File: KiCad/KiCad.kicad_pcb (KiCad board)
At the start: 2 copper layers, 43 parts, among them J1 Conn_01x03, J2 Conn_01x03, J3 Conn_01x03, J4 Screw_Terminal_01x02, J5 Screw_Terminal_01x02, Q1 2N3906, Q2 2N3906, Q3 2N3906, Q4 2N3904, Q5 2N3904, Q6 2N3904, U2 L298HN, U3 L7805, U4 ARDUINO_MKR_WAN_1310

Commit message: q
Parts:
- added C10: 0.1u, Capacitor_SMD:C_1206_3216Metric_Pad1.33x1.80mm_HandSolder, F.Cu at (131.7, 118.4)
- added C11: 0.1u, Capacitor_SMD:C_1206_3216Metric_Pad1.33x1.80mm_HandSolder, F.Cu at (131.7, 121.7)
- added C12: 0.1u, Capacitor_SMD:C_1206_3216Metric_Pad1.33x1.80mm_HandSolder, F.Cu at (131.7, 125.1)
- added C13: 0.1u, Capacitor_SMD:C_1206_3216Metric_Pad1.33x1.80mm_HandSolder, F.Cu at (131.7, 128.4)
- added C14: 0.1u, Capacitor_SMD:C_1206_3216Metric_Pad1.33x1.80mm_HandSolder, F.Cu at (131.7, 131.8)
- added C5: 0.1u, Capacitor_SMD:C_1206_3216Metric_Pad1.33x1.80mm_HandSolder, F.Cu at (125.7, 125.1)
- added C6: 0.1u, Capacitor_SMD:C_1206_3216Metric_Pad1.33x1.80mm_HandSolder, F.Cu at (125.7, 128.4)
- added C7: 0.1u, Capacitor_SMD:C_1206_3216Metric_Pad1.33x1.80mm_HandSolder, F.Cu at (125.7, 131.8)
- added C8: 0.1u, Capacitor_SMD:C_1206_3216Metric_Pad1.33x1.80mm_HandSolder, F.Cu at (131.7, 111.7)
- added C9: 0.1u, Capacitor_SMD:C_1206_3216Metric_Pad1.33x1.80mm_HandSolder, F.Cu at (131.7, 115.0)
- added D11: 1N5711UR, Diode_SMD:D_1206_3216Metric_Pad1.42x1.75mm_HandSolder, F.Cu at (148.8, 104.0)
- added D12: 1N5711UR, Diode_SMD:D_1206_3216Metric_Pad1.42x1.75mm_HandSolder, F.Cu at (148.8, 107.3)
- added D13: 1N4007, Diode_SMD:D_1206_3216Metric_Pad1.42x1.75mm_HandSolder, F.Cu at (148.8, 110.7)
- added D14: 1N4007, Diode_SMD:D_1206_3216Metric_Pad1.42x1.75mm_HandSolder, F.Cu at (148.8, 114.1)
- added D15: 1N4007, Diode_SMD:D_1206_3216Metric_Pad1.42x1.75mm_HandSolder, F.Cu at (148.8, 117.5)
- added D16: 1N4007, Diode_SMD:D_1206_3216Metric_Pad1.42x1.75mm_HandSolder, F.Cu at (148.8, 120.9)
- added D17: 1N4007, Diode_SMD:D_1206_3216Metric_Pad1.42x1.75mm_HandSolder, F.Cu at (148.8, 124.3)
- added D18: 1N4007, Diode_SMD:D_1206_3216Metric_Pad1.42x1.75mm_HandSolder, F.Cu at (148.8, 127.7)
- added D19: 1N4007, Diode_SMD:D_1206_3216Metric_Pad1.42x1.75mm_HandSolder, F.Cu at (154.8, 100.6)
- added D20: 1N4007, Diode_SMD:D_1206_3216Metric_Pad1.42x1.75mm_HandSolder, F.Cu at (154.8, 104.0)
- added D21: 1N4007, Diode_SMD:D_1206_3216Metric_Pad1.42x1.75mm_HandSolder, F.Cu at (154.8, 107.3)
- added D22: 1N4007, Diode_SMD:D_1206_3216Metric_Pad1.42x1.75mm_HandSolder, F.Cu at (154.8, 110.7)
- added D23: 1N4007, Diode_SMD:D_1206_3216Metric_Pad1.42x1.75mm_HandSolder, F.Cu at (154.8, 114.1)
- added D24: 1N4007, Diode_SMD:D_1206_3216Metric_Pad1.42x1.75mm_HandSolder, F.Cu at (154.8, 117.5)
- added D25: 1N4007, Diode_SMD:D_1206_3216Metric_Pad1.42x1.75mm_HandSolder, F.Cu at (154.8, 120.9)
- added D26: 1N4007, Diode_SMD:D_1206_3216Metric_Pad1.42x1.75mm_HandSolder, F.Cu at (154.8, 124.3)
- added D27: 1N4007, Diode_SMD:D_1206_3216Metric_Pad1.42x1.75mm_HandSolder, F.Cu at (154.8, 127.7)
- added D28: 1N4007, Diode_SMD:D_1206_3216Metric_Pad1.42x1.75mm_HandSolder, F.Cu at (160.8, 100.6)
- added D29: 1N4007, Diode_SMD:D_1206_3216Metric_Pad1.42x1.75mm_HandSolder, F.Cu at (160.8, 104.0)
- added D30: 1N4007, Diode_SMD:D_1206_3216Metric_Pad1.42x1.75mm_HandSolder, F.Cu at (160.8, 107.3)
- added D31: 1N4007, Diode_SMD:D_1206_3216Metric_Pad1.42x1.75mm_HandSolder, F.Cu at (160.8, 110.7)
- added D32: 1N4007, Diode_SMD:D_1206_3216Metric_Pad1.42x1.75mm_HandSolder, F.Cu at (160.8, 114.1)
- added D33: 1N4007, Diode_SMD:D_1206_3216Metric_Pad1.42x1.75mm_HandSolder, F.Cu at (160.8, 117.5)
- added D34: 1N4007, Diode_SMD:D_1206_3216Metric_Pad1.42x1.75mm_HandSolder, F.Cu at (160.8, 120.9)
- added D35: 1N4007, Diode_SMD:D_1206_3216Metric_Pad1.42x1.75mm_HandSolder, F.Cu at (160.8, 124.3)
- added D36: 1N4007, Diode_SMD:D_1206_3216Metric_Pad1.42x1.75mm_HandSolder, F.Cu at (160.8, 127.7)
- added D37: 1N4007, Diode_SMD:D_1206_3216Metric_Pad1.42x1.75mm_HandSolder, F.Cu at (166.8, 100.6)
- added D38: 1N4007, Diode_SMD:D_1206_3216Metric_Pad1.42x1.75mm_HandSolder, F.Cu at (166.8, 104.0)
- added D39: 1N4007, Diode_SMD:D_1206_3216Metric_Pad1.42x1.75mm_HandSolder, F.Cu at (166.8, 107.3)
- added D40: 1N4007, Diode_SMD:D_1206_3216Metric_Pad1.42x1.75mm_HandSolder, F.Cu at (166.8, 110.7)
- added D41: 1N5711UR, Diode_SMD:D_1206_3216Metric_Pad1.42x1.75mm_HandSolder, F.Cu at (166.8, 114.1)
- added D42: 1N5711UR, Diode_SMD:D_1206_3216Metric_Pad1.42x1.75mm_HandSolder, F.Cu at (166.8, 117.5)
- added IC2: MCP23017-E_SO, SamacSys_Parts:SOIC127P1030X265-28N, F.Cu at (176.1, 108.6)
- added IC3: MCP23017-E_SO, SamacSys_Parts:SOIC127P1030X265-28N, F.Cu at (188.8, 108.6)
- added J10: Screw_Terminal_01x02, TerminalBlock_Phoenix:TerminalBlock_Phoenix_MKDS-1,5-2_1x02_P5.00mm_Horizontal, F.Cu at (177.1, 56.9)
- added J11: Screw_Terminal_01x02, TerminalBlock_Phoenix:TerminalBlock_Phoenix_MKDS-1,5-2_1x02_P5.00mm_Horizontal, F.Cu at (177.1, 68.8)
- added J12: Screw_Terminal_01x02, TerminalBlock_Phoenix:TerminalBlock_Phoenix_MKDS-1,5-2_1x02_P5.00mm_Horizontal, F.Cu at (177.1, 80.7)
- added J13: Screw_Terminal_01x02, TerminalBlock_Phoenix:TerminalBlock_Phoenix_MKDS-1,5-2_1x02_P5.00mm_Horizontal, F.Cu at (177.1, 92.5)
- added J14: Screw_Terminal_01x02, TerminalBlock_Phoenix:TerminalBlock_Phoenix_MKDS-1,5-2_1x02_P5.00mm_Horizontal, F.Cu at (189.1, 56.9)
- added J15: Screw_Terminal_01x02, TerminalBlock_Phoenix:TerminalBlock_Phoenix_MKDS-1,5-2_1x02_P5.00mm_Horizontal, F.Cu at (189.1, 68.8)
- added J16: Screw_Terminal_01x02, TerminalBlock_Phoenix:TerminalBlock_Phoenix_MKDS-1,5-2_1x02_P5.00mm_Horizontal, F.Cu at (189.1, 80.7)
- added J18: Screw_Terminal_01x04, TerminalBlock_Phoenix:TerminalBlock_Phoenix_MKDS-1,5-4_1x04_P5.00mm_Horizontal, F.Cu at (143.3, 135.6)
- added J6: Screw_Terminal_01x03, TerminalBlock_Phoenix:TerminalBlock_Phoenix_MKDS-1,5-3_1x03_P5.00mm_Horizontal, F.Cu at (126.2, 92.5)
- added J7: Screw_Terminal_01x02, TerminalBlock_Phoenix:TerminalBlock_Phoenix_MKDS-1,5-2_1x02_P5.00mm_Horizontal, F.Cu at (165.0, 80.7)
- added J8: Screw_Terminal_01x03, TerminalBlock_Phoenix:TerminalBlock_Phoenix_MKDS-1,5-3_1x03_P5.00mm_Horizontal, F.Cu at (126.2, 104.4)
- added J9: Screw_Terminal_01x02, TerminalBlock_Phoenix:TerminalBlock_Phoenix_MKDS-1,5-2_1x02_P5.00mm_Horizontal, F.Cu at (165.0, 92.5)
- added Q10: 2N3904, Package_TO_SOT_SMD:SOT-23, F.Cu at (103.5, 141.3)
- added Q7: 2N3906, Package_TO_SOT_SMD:SOT-23, F.Cu at (103.5, 127.9)
- added Q8: 2N3904, Package_TO_SOT_SMD:SOT-23, F.Cu at (103.5, 132.4)
- added Q9: 2N3906, Package_TO_SOT_SMD:SOT-23, F.Cu at (103.5, 136.8)
- added R16: PAD, Resistor_SMD:R_1206_3216Metric_Pad1.30x1.75mm_HandSolder, F.Cu at (184.6, 123.2)
- added R17: PAD, Resistor_SMD:R_1206_3216Metric_Pad1.30x1.75mm_HandSolder, F.Cu at (184.6, 126.5)
- added R18: 1.7k, Resistor_SMD:R_1206_3216Metric_Pad1.30x1.75mm_HandSolder, F.Cu at (184.6, 129.8)
- added R19: 3.3k, Resistor_SMD:R_1206_3216Metric_Pad1.30x1.75mm_HandSolder, F.Cu at (184.6, 133.1)
- added R20: 4.7k, Resistor_SMD:R_1206_3216Metric_Pad1.30x1.75mm_HandSolder, F.Cu at (184.6, 136.4)
- added R21: 10k, Resistor_SMD:R_1206_3216Metric_Pad1.30x1.75mm_HandSolder, F.Cu at (184.6, 139.7)
- added R22: 27k, Resistor_SMD:R_1206_3216Metric_Pad1.30x1.75mm_HandSolder, F.Cu at (190.6, 120.0)
- added R23: 1.7k, Resistor_SMD:R_1206_3216Metric_Pad1.30x1.75mm_HandSolder, F.Cu at (190.6, 123.2)
- added R24: 3.3k, Resistor_SMD:R_1206_3216Metric_Pad1.30x1.75mm_HandSolder, F.Cu at (190.6, 126.5)
- added R25: 4.7k, Resistor_SMD:R_1206_3216Metric_Pad1.30x1.75mm_HandSolder, F.Cu at (190.6, 129.8)
- added R26: 10k, Resistor_SMD:R_1206_3216Metric_Pad1.30x1.75mm_HandSolder, F.Cu at (190.6, 133.1)
- added R27: 27k, Resistor_SMD:R_1206_3216Metric_Pad1.30x1.75mm_HandSolder, F.Cu at (190.6, 136.4)
- added U1: L298HN, Package_TO_SOT_THT:TO-220-15_P2.54x2.54mm_StaggerOdd_Lead4.58mm_Vertical, F.Cu at (141.7, 61.1)
- added U5: L298HN, Package_TO_SOT_THT:TO-220-15_P2.54x2.54mm_StaggerOdd_Lead4.58mm_Vertical, F.Cu at (141.7, 85.1)
- added U6: L298HN, Package_TO_SOT_THT:TO-220-15_P2.54x2.54mm_StaggerOdd_Lead4.58mm_Vertical, F.Cu at (141.7, 97.2)
- added U7: LM75AIMX_NOPB, SamacSys_Parts:SOIC127P600X175-8N, F.Cu at (110.2, 130.5)
- J1, J2, J3: value Conn_01x03 -> Screw_Terminal_01x03; footprint Connector_PinHeader_1.27mm:PinHeader_1x03_P1.27mm_Vertical -> TerminalBlock_Phoenix:TerminalBlock_Phoenix_MKDS-1,5-3_1x03_P5.00mm_Horizontal
- moved Q1 95.0 mm to (98.6, 123.5)
- moved Q2 95.0 mm to (98.6, 127.9)
- moved Q3 95.0 mm to (98.6, 132.4)
- moved Q4 95.0 mm to (98.6, 136.8)
- moved Q5 95.0 mm to (98.6, 141.3)
- moved Q6 79.8 mm to (103.5, 123.5)
- moved C1 70.9 mm to (125.7, 111.7)
- moved C2 70.9 mm to (125.7, 115.0)
- moved C3 70.9 mm to (125.7, 118.4)
- moved C4 70.9 mm to (125.7, 121.7)
- moved U3 58.0 mm to (109.2, 125.2)
- moved J4 52.9 mm to (165.0, 56.9)
- moved J5 52.9 mm to (165.0, 68.8)
- moved U2 46.2 mm to (141.7, 73.1)
- moved D1 42.7 mm to (142.8, 100.6)
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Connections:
- D1 pad 2: /S3_IN -> /S_HUM_1_IN
- D2 pad 1: /S3_IN -> /S_HUM_1_IN
- D3 pad 2: /S4_IN -> /S_HUM_2_IN
- D4 pad 1: /S4_IN -> /S_HUM_2_IN
- D5 pad 2: /S5_IN -> /S_HUM_3_IN
- D6 pad 1: /S5_IN -> /S_HUM_3_IN
- R1 pad 2: /S3_IN -> /S_HUM_1_IN
- R10 pad 2: +3V3 -> +3.3V
- R13 pad 2: /S1_EN -> /S_HUM_1_EN
- R14 pad 2: /S4_EN -> /S_HUM_2_EN
- R15 pad 2: /S5_EN -> /S_HUM_3_EN
- R2 pad 1: /S3_IN -> /S_HUM_1_IN
- R3 pad 2: /S4_IN -> /S_HUM_2_IN
- R4 pad 1: /S4_IN -> /S_HUM_2_IN
- R5 pad 2: /S5_IN -> /S_HUM_3_IN
- R6 pad 1: /S5_IN -> /S_HUM_3_IN
- U2 pad 1: unconnected-(U2-SENSE_A-Pad1) -> Earth
- U2 pad 10: /D2_IN -> /P2_IN2
- U2 pad 11: /D_EN -> /P2_EN
- U2 pad 12: /D1_IN -> /P2_IN1
- U2 pad 2: unconnected-(U2-OUT1-Pad2) -> Net-(D15-A)
- U2 pad 3: unconnected-(U2-OUT2-Pad3) -> Net-(D13-A)
- U2 pad 5: unconnected-(U2-IN1-Pad5) -> /P1_IN2
- U2 pad 6: unconnected-(U2-EnA-Pad6) -> /P1_EN
- U2 pad 7: unconnected-(U2-IN2-Pad7) -> /P1_IN1
- U4 pad J3_1: /S3_IN -> /S_HUM_2_IN
- U4 pad J3_10: unconnected-(U4-PA23/D1(PWM)-PadJ3_10) -> /S_HUM_2_EN
- U4 pad J3_11: unconnected-(U4-PA10/D2(PWM)-PadJ3_11) -> /S_HUM_3_EN
- U4 pad J3_12: unconnected-(U4-PA11/D3(PWM)-PadJ3_12) -> /S_ILUM_EN
- U4 pad J3_13: unconnected-(U4-PB10/D4(PWM)-PadJ3_13) -> /S_ANEM_EN
- U4 pad J3_14: unconnected-(U4-PB11/D5(PWM)-PadJ3_14) -> /FOCO_EN
- U4 pad J3_2: unconnected-(U4-PA02/D15/DAC0/AIN(0)/A0-PadJ3_2) -> /S_HUM_1_IN
- U4 pad J3_5: /S4_IN -> /S_HUM_3_IN
- U4 pad J3_6: /S5_IN -> /S_ILUM_IN
- U4 pad J3_7: unconnected-(U4-PA06/D20/AIN(6)/A5-PadJ3_7) -> /S_ANEM_IN
- U4 pad J3_9: /S3_EN -> /S_HUM_1_EN
- U4 pad J5_1: unconnected-(U4-PA20/D6(PWM)-PadJ5_1) -> /HEAT_EN
- U4 pad J5_12: +3V3 -> +3.3V
- U4 pad J5_6: unconnected-(U4-PA08/D11/SDA(SC2)-PadJ5_6) -> /SDA
- U4 pad J5_7: unconnected-(U4-PA09/D12(PWM)/SCL(SC2)-PadJ5_7) -> /SCL

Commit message: sch done
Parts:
- removed IC3: MCP23017-E_SO, SamacSys_Parts:SOIC127P1030X265-28N
- removed J18: Screw_Terminal_01x04, TerminalBlock_Phoenix:TerminalBlock_Phoenix_MKDS-1,5-4_1x04_P5.00mm_Horizontal
- added C15: 0.1u, Capacitor_SMD:C_1206_3216Metric_Pad1.33x1.80mm_HandSolder, F.Cu at (189.1, 62.6)
- added IC1: MCP23017-E_SO, SamacSys_Parts:SOIC127P1030X265-28N, F.Cu at (150.8, -41.5)
- added J17: Screw_Terminal_01x04, TerminalBlock_Phoenix:TerminalBlock_Phoenix_MKDS-1,5-4_1x04_P5.00mm_Horizontal, F.Cu at (194.6, 99.5)
- C14: value 0.1u -> 0.33u
- C4: value 0.33u -> 0.1u
- D10, D7, D8, D9: value 1N4007 -> 1N5711UR
- D11, D12, D41, D42: value 1N5711UR -> 1N4007
- J12: value Screw_Terminal_01x02 -> Screw_Terminal_01x05; footprint TerminalBlock_Phoenix:TerminalBlock_Phoenix_MKDS-1,5-2_1x02_P5.00mm_Horizontal -> TerminalBlock_Phoenix:TerminalBlock_Phoenix_MKDS-1,5-5_1x05_P5.00mm_Horizontal
- J4, J5: value Screw_Terminal_01x02 -> Screw_Terminal_01x03; footprint TerminalBlock_Phoenix:TerminalBlock_Phoenix_MKDS-1,5-2_1x02_P5.00mm_Horizontal -> TerminalBlock_Phoenix:TerminalBlock_Phoenix_MKDS-1,5-3_1x03_P5.00mm_Horizontal
- J6, J8: value Screw_Terminal_01x03 -> Screw_Terminal_01x02; footprint TerminalBlock_Phoenix:TerminalBlock_Phoenix_MKDS-1,5-3_1x03_P5.00mm_Horizontal -> TerminalBlock_Phoenix:TerminalBlock_Phoenix_MKDS-1,5-2_1x02_P5.00mm_Horizontal
- Q4, Q5: value 2N3904 -> 2N3906
- Q7, Q9: value 2N3906 -> 2N3904
- R10: value 10k -> 3.3k
- R11, R12: value 10k -> 4.7k
- R13, R14, R15: value 27k -> 4.7k
- R16, R17: value PAD -> 10k
- R18: value 1.7k -> 10k
- R19: value 3.3k -> 10k
- R20: value 4.7k -> 10k
- R21: value 10k -> 27k
- R23: value 1.7k -> 27k
- R24: value 3.3k -> 27k
- R25: value 4.7k -> 27k
- R26: value 10k -> PAD
- R27: value 27k -> PAD
- R7, R9: value 4.7k -> 1.7k
- R8: value 4.7k -> 3.3k
- U2: value L298HN -> ARDUINO_MKR_WAN_1310; footprint Package_TO_SOT_THT:TO-220-15_P2.54x2.54mm_StaggerOdd_Lead4.58mm_Vertical -> SimbolosSnapEDA:BOARD_ARDUINO_MKR_WAN_1310
- U3: value L7805 -> L298HN; footprint Package_TO_SOT_THT:TO-220-3_Vertical -> Package_TO_SOT_THT:TO-220-15_P2.54x2.54mm_StaggerOdd_Lead4.58mm_Vertical
- U4: value ARDUINO_MKR_WAN_1310 -> L298HN; footprint SimbolosSnapEDA:BOARD_ARDUINO_MKR_WAN_1310 -> Package_TO_SOT_THT:TO-220-15_P2.54x2.54mm_StaggerOdd_Lead4.58mm_Vertical
- U6: value L298HN -> LM75AIMX_NOPB; footprint Package_TO_SOT_THT:TO-220-15_P2.54x2.54mm_StaggerOdd_Lead4.58mm_Vertical -> SamacSys_Parts:SOIC127P600X175-8N
- U7: value LM75AIMX_NOPB -> L7805; footprint SamacSys_Parts:SOIC127P600X175-8N -> Package_TO_SOT_THT:TO-220-3_Vertical
- moved R22 170.5 mm to (36.1, 47.7)
- moved R17 166.4 mm to (35.4, 52.9)
- moved IC2 163.3 mm to (112.9, -42.0)
- moved J5 163.2 mm to (22.9, 148.9)
- moved R12 162.1 mm to (35.4, 57.2)
- moved R3 161.0 mm to (29.5, 53.0)
- moved R4 161.0 mm to (29.5, 56.3)
- moved R23 155.1 mm to (39.8, 86.7)
- moved R18 153.7 mm to (35.7, 92.1)
- moved R25 152.7 mm to (41.1, 161.0)
- moved R20 152.7 mm to (35.1, 167.6)
- moved R24 151.6 mm to (39.0, 129.2)
- moved R8 151.6 mm to (27.1, 122.6)
- moved J4 151.4 mm to (23.9, 111.7)
- moved C11 149.0 mm to (203.7, -8.73)
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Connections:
- C1 pad 1: +5V -> +12V
- C11 pad 1: +5V -> +12V
- C12 pad 1: +12V -> +5V
- C13 pad 1: +12V -> /Vin
- C14 pad 1: +5V -> Net-(J16-Pin_2)
- C3 pad 1: /Vin -> +5V
- C4 pad 1: Net-(J5-Pin_2) -> +12V
- C6 pad 1: +12V -> +5V
- C8 pad 1: +5V -> +12V
- C9 pad 1: +12V -> +5V
- D10 pad 1: Net-(D10-K) -> /S_ANEM_IN
- D11 pad 1: +3V3 -> +12V
- D11 pad 2: /S_ILUM_IN -> Net-(D11-A)
- D12 pad 1: /S_ILUM_IN -> Net-(D11-A)
- D41 pad 1: +3V3 -> +12V
- D41 pad 2: /S_ANEM_IN -> Net-(D41-A)
- D42 pad 1: /S_ANEM_IN -> Net-(D41-A)
- D7 pad 1: +12V -> +3V3
- D7 pad 2: Net-(D7-A) -> /S_ILUM_IN
- D8 pad 1: Net-(D7-A) -> /S_ILUM_IN
- D9 pad 1: +12V -> +3V3
- D9 pad 2: Net-(D10-K) -> /S_ANEM_IN
- IC2 pad 15: Earth -> +3.3V
- J10 pad 1: Net-(D15-A) -> /HEAT_EN
- J10 pad 2: Net-(D13-A) -> Earth
- J11 pad 1: Net-(D19-A) -> Net-(D29-A)
- J11 pad 2: Net-(D17-A) -> Net-(D27-A)
- J12 pad 1: Net-(D23-A) -> /FOCO1_EN
- J12 pad 2: Net-(D21-A) -> /FOCO2_EN
- J13 pad 1: Net-(D27-A) -> Net-(D33-A)
- J13 pad 2: Net-(D25-A) -> Net-(D31-A)
- J14 pad 1: Net-(D31-A) -> Net-(D37-A)
- J14 pad 2: Net-(D29-A) -> Net-(D35-A)
- J15 pad 1: Net-(D35-A) -> Net-(D41-A)
- J15 pad 2: Net-(D33-A) -> Net-(D39-A)
- J16 pad 1: Net-(D39-A) -> Earth
- J16 pad 2: Net-(D37-A) -> Net-(J16-Pin_2)
- J4 pad 1: Net-(D10-K) -> Net-(J4-Pin_1)
- J4 pad 2: Net-(D7-A) -> Net-(J4-Pin_2)
- J5 pad 1: Earth -> Net-(J5-Pin_1)
- J6 pad 1: Net-(J6-Pin_1) -> Net-(D13-A)
- J6 pad 2: Net-(J6-Pin_2) -> Net-(D11-A)
- J7 pad 1: /FOCO_EN -> Net-(D17-A)
- J7 pad 2: Earth -> Net-(D15-A)
- J8 pad 1: Net-(J8-Pin_1) -> Net-(D21-A)
- J8 pad 2: Net-(J8-Pin_2) -> Net-(D19-A)
- J9 pad 1: /HEAT_EN -> Net-(D25-A)
- J9 pad 2: Earth -> Net-(D23-A)
- Q4 pad 1: Earth -> +5V
- Q4 pad 3: Net-(Q4-C) -> Net-(J4-Pin_1)
- Q5 pad 1: Earth -> +5V
- Q5 pad 3: Net-(Q5-C) -> Net-(J5-Pin_1)
- Q7 pad 1: +5V -> Earth
- Q7 pad 3: Net-(J6-Pin_1) -> Net-(Q7-C)
- Q9 pad 1: +5V -> Earth
- Q9 pad 3: Net-(J8-Pin_1) -> Net-(Q9-C)
- R10 pad 1: Net-(Q4-C) -> /S_ANEM_IN
- R10 pad 2: +3.3V -> Earth
- R11 pad 1: Net-(Q5-C) -> Net-(Q6-C)
- R11 pad 2: +3V3 -> Net-(Q1-B)
- R12 pad 1: Net-(Q6-C) -> Net-(Q7-C)
- R12 pad 2: +3V3 -> Net-(Q2-B)
- R13 pad 1: Net-(Q4-B) -> Net-(Q8-C)
- R13 pad 2: /S_HUM_1_EN -> Net-(Q3-B)
- R14 pad 1: Net-(Q5-B) -> Net-(Q9-C)
- R14 pad 2: /S_HUM_2_EN -> Net-(Q4-B)
- R15 pad 1: Net-(Q6-B) -> Net-(Q10-C)
- R15 pad 2: /S_HUM_3_EN -> Net-(Q5-B)
- R16 pad 1: +5V -> Net-(Q6-C)
- R16 pad 2: /SDA -> +3.3V
- R17 pad 1: /SCL -> Net-(Q7-C)
- R17 pad 2: +5V -> +3V3
- R18 pad 1: Net-(J6-Pin_2) -> Net-(Q8-C)
- R18 pad 2: /S_ILUM_IN -> +3V3
- R19 pad 1: /S_ILUM_IN -> Net-(Q9-C)
- R19 pad 2: Earth -> +3V3
- R20 pad 1: Net-(Q8-C) -> Net-(Q10-C)
- R20 pad 2: Net-(Q7-B) -> +3V3
- R21 pad 1: Net-(Q8-C) -> Net-(Q6-B)
- R21 pad 2: +3V3 -> /S_HUM_1_EN
- R22 pad 1: Net-(Q8-B) -> Net-(Q7-B)
- R22 pad 2: /S_ILUM_EN -> /S_HUM_2_EN
- R23 pad 1: Net-(J8-Pin_2) -> Net-(Q8-B)
- R23 pad 2: /S_ANEM_IN -> /S_HUM_3_EN
- R24 pad 1: /S_ANEM_IN -> Net-(Q9-B)
- R24 pad 2: Earth -> /S_ILUM_EN
- R25 pad 1: Net-(Q10-C) -> Net-(Q10-B)
- R25 pad 2: Net-(Q9-B) -> /S_ANEM_EN
- R26 pad 1: Net-(Q10-C) -> +5V
- R26 pad 2: +3V3 -> /SDA
- R27 pad 1: Net-(Q10-B) -> /SCL
- R27 pad 2: /S_ANEM_EN -> +5V
- R7 pad 1: Net-(Q4-C) -> Net-(J4-Pin_2)
- R7 pad 2: Net-(Q1-B) -> /S_ILUM_IN
- R8 pad 1: Net-(Q5-C) -> /S_ILUM_IN
- R8 pad 2: Net-(Q2-B) -> Earth
- R9 pad 1: Net-(Q6-C) -> Net-(J5-Pin_2)
- R9 pad 2: Net-(Q3-B) -> /S_ANEM_IN
- U1 pad 10: /P4_IN2 -> /R1_IN2
- U1 pad 11: /P4_EN -> /R1_EN
- U1 pad 12: /P4_IN1 -> /R1_IN1
- U1 pad 13: Net-(D19-A) -> Net-(D13-A)
- U1 pad 14: Net-(D17-A) -> Net-(D11-A)
- U1 pad 2: Net-(D23-A) -> Net-(D17-A)
- U1 pad 3: Net-(D21-A) -> Net-(D15-A)
- U1 pad 5: /P3_IN2 -> /W2_IN2
- U1 pad 6: /P3_EN -> /W2_EN
- U1 pad 7: /P3_IN1 -> /W2_IN1
- U3 pad 1: Net-(J5-Pin_2) -> Earth
- U3 pad 2: Earth -> Net-(D25-A)
- U3 pad 3: /Vin -> Net-(D23-A)
- U5 pad 10: /W1_IN2 -> /P2_IN2
- U5 pad 11: /W1_EN -> /P2_EN
- U5 pad 12: /W1_IN1 -> /P2_IN1
- U5 pad 13: Net-(D27-A) -> Net-(D37-A)
- U5 pad 14: Net-(D25-A) -> Net-(D35-A)
- U5 pad 2: Net-(D31-A) -> Net-(D41-A)
- U5 pad 3: Net-(D29-A) -> Net-(D39-A)
- U5 pad 5: /P5_IN2 -> /P1_IN2
- U5 pad 6: /P5_EN -> /P1_EN
- U5 pad 7: /P5_IN1 -> /P1_IN1
- U6 pad 1: Earth -> /SDA
- U6 pad 2: Net-(D39-A) -> /SCL
- U6 pad 3: Net-(D37-A) -> unconnected-(U6-O.S.-Pad3)
- U6 pad 4: +12V -> Earth
- U6 pad 5: /W2_IN2 -> Earth
- U6 pad 6: /W2_EN -> Earth
- U6 pad 7: /W2_IN1 -> Earth
- U6 pad 8: Earth -> +5V
- U7 pad 1: /SDA -> Net-(J16-Pin_2)
- U7 pad 2: /SCL -> Earth
- U7 pad 3: unconnected-(U7-O.S.-Pad3) -> /Vin
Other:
- board outline added: 100 x 100 mm

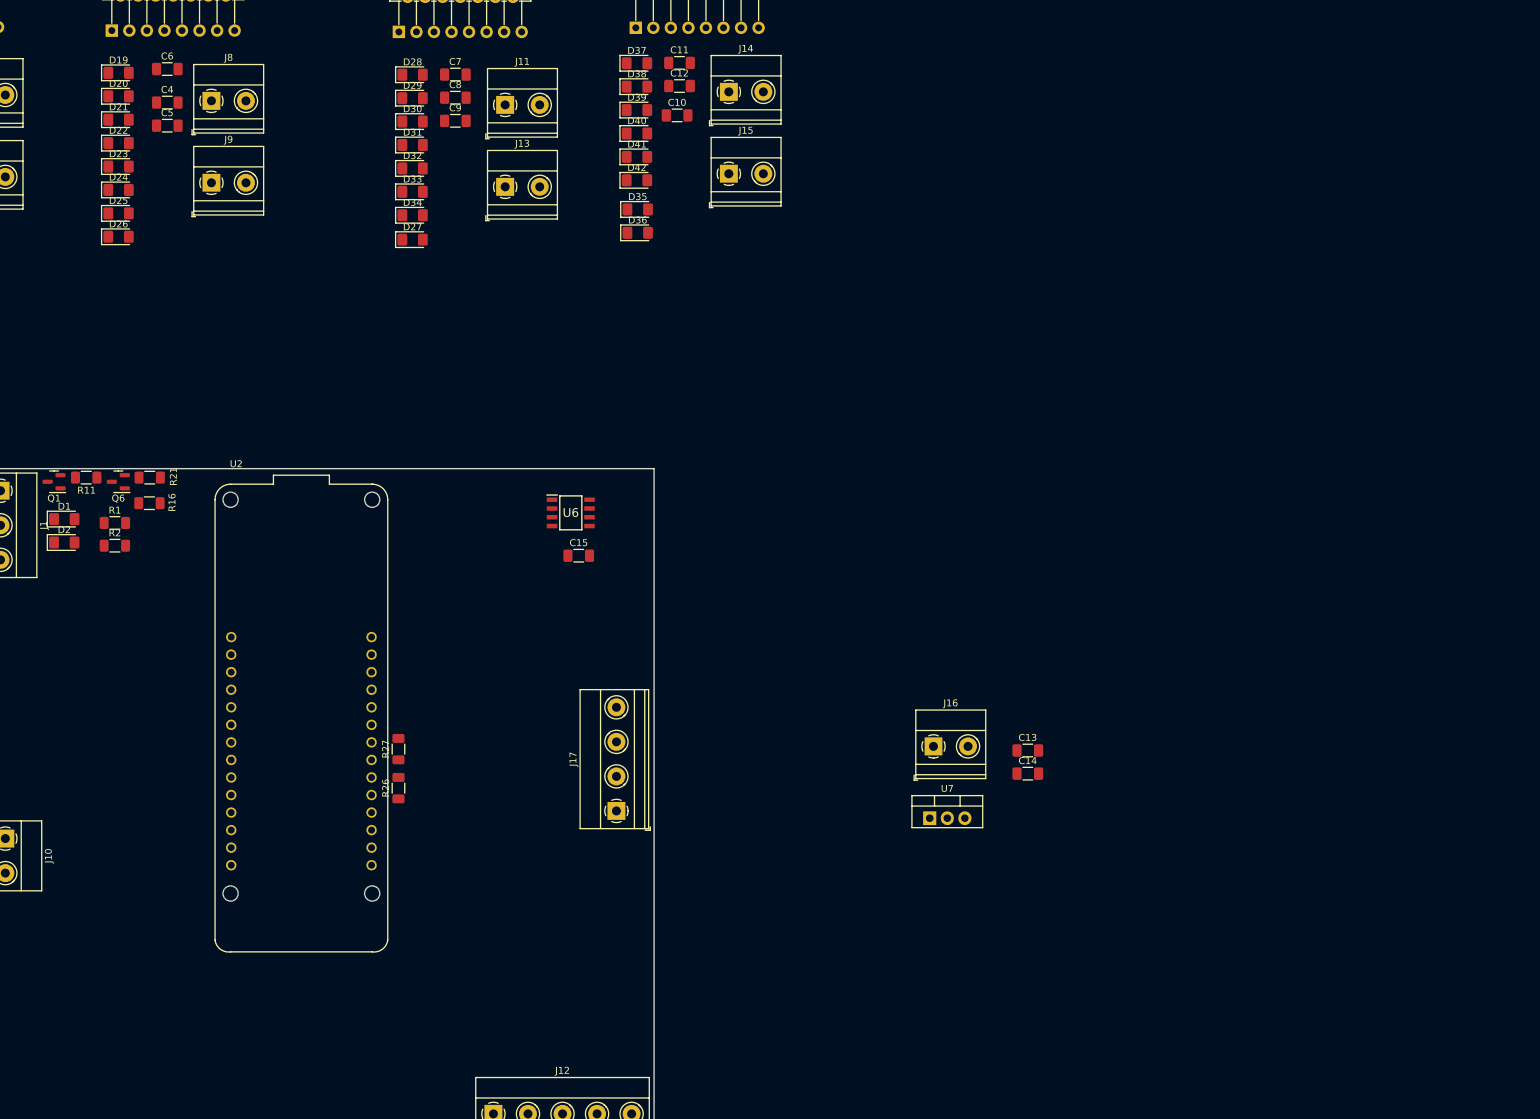
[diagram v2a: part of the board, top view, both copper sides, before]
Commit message: added missing footprints
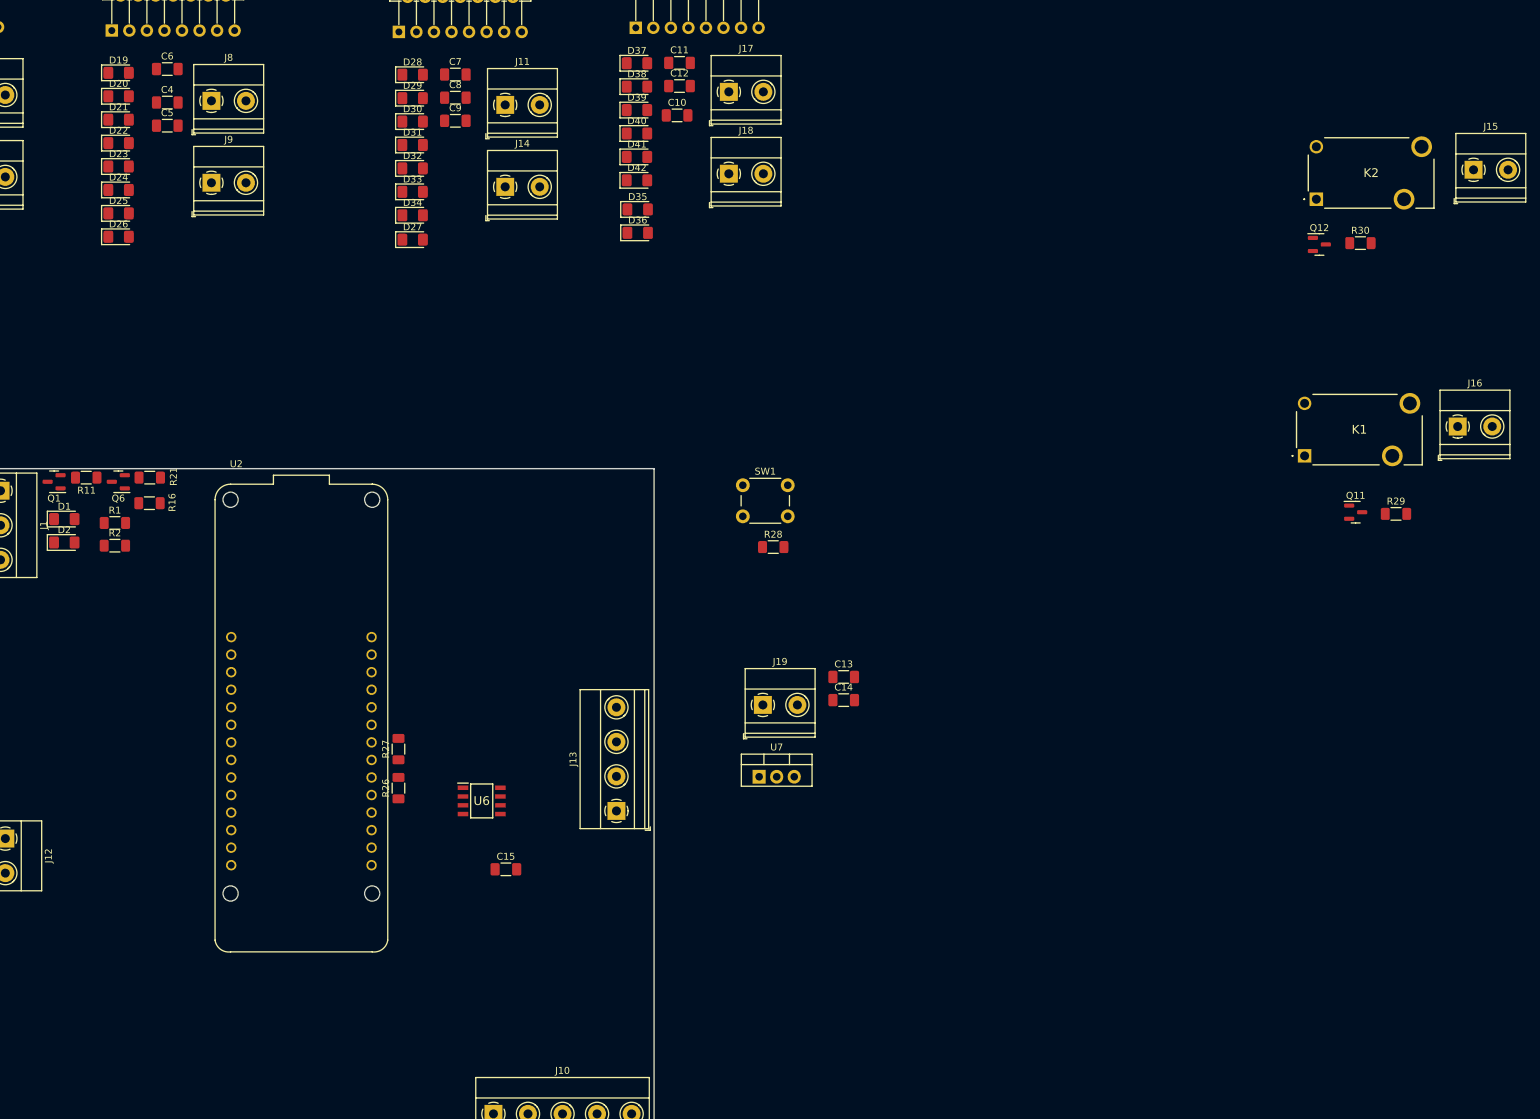
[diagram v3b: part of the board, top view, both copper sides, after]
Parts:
- added J15: Screw_Terminal_01x02, TerminalBlock_Phoenix:TerminalBlock_Phoenix_MKDS-1,5-2_1x02_P5.00mm_Horizontal, F.Cu at (318.6, 6.74)
- added J16: Screw_Terminal_01x02, TerminalBlock_Phoenix:TerminalBlock_Phoenix_MKDS-1,5-2_1x02_P5.00mm_Horizontal, F.Cu at (316.3, 43.9)
- added K1: 2071556-9, SamacSys_Parts:20715569, F.Cu at (294.2, 48.1)
- added K2: 2071556-9, SamacSys_Parts:20715569, F.Cu at (295.9, 11.0)
- added Q11: 2N3904, Package_TO_SOT_SMD:SOT-23, F.Cu at (301.6, 56.3)
- added Q12: 2N3904, Package_TO_SOT_SMD:SOT-23, F.Cu at (296.3, 17.6)
- added R28: 10k, Resistor_SMD:R_1206_3216Metric_Pad1.30x1.75mm_HandSolder, F.Cu at (217.2, 61.4)
- added R29: 1.5k, Resistor_SMD:R_1206_3216Metric_Pad1.30x1.75mm_HandSolder, F.Cu at (307.4, 56.5)
- added R30: 1.5k, Resistor_SMD:R_1206_3216Metric_Pad1.30x1.75mm_HandSolder, F.Cu at (302.2, 17.4)
- added SW1: SW_Push, Button_Switch_THT:SW_PUSH_6mm_H4.3mm, F.Cu at (212.8, 52.4)
- moved C15 46.6 mm to (178.6, 108.0)
- moved U6 43.6 mm to (175.1, 98.1)
- moved C14 28.7 mm to (227.4, 83.5)
- moved C13 28.7 mm to (227.4, 80.2)
- moved J19 25.4 mm to (215.8, 84.2)
- moved U7 25.4 mm to (215.2, 94.6)
- renumbered J12 to J10, J10 to J12, J17 to J13, J13 to J14, J14 to J17, J15 to J18, J16 to J19
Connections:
- net /FOCO1_EN renamed /FOCO_1_EN
- net /FOCO2_EN renamed /FOCO_2_EN
- net /FOCO3_EN renamed /FOCO_3_EN
- net /FOCO4_EN renamed /FOCO_4_EN
- IC2 pad 27: unconnected-(IC2-GPA6-Pad27) -> /RELAY_2_EN
- IC2 pad 28: unconnected-(IC2-GPA7-Pad28) -> /RELAY_1_EN
- U2 pad J3_7: unconnected-(U2-PA06/D20/AIN(6)/A5-PadJ3_7) -> /PULSE_IN
